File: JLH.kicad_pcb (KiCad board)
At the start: 2 copper layers, 170 x 200 mm, 51 parts, among them J1 Вход, J2 Выход, J3 B2P-VH, Q1 КТ361Г, Q2 КТ801А, Q3 2Т803А, Q4 2Т803А, Q5 КТ361Г, Q6 КТ801А, Q7 2Т803А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

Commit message: Fixed polarity
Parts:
- moved R1 25.1 mm to (87.6, 137.5), turned to 90 degrees
- moved J3 14.8 mm to (76.2, 137.5), turned to 90 degrees
- moved D1 14.5 mm to (73.7, 122.3)
- moved C13 5.00 mm to (102.0, 133.5)
- moved C6 5.00 mm to (102.0, 118.5)
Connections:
- J3 pad 1: /Левый канал/VCC -> GND
- J3 pad 2: GND -> /Левый канал/VCC
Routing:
- net GND: track 666.0 -> 78.9 mm
- net /Левый канал/VCC: track 593.0 -> 575.8 mm
- net Net-(D1-Pad2): track 4.72 -> 11.4 mm
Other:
- board text added: "Левый +"
- board text added: "Левый -"
- board text added: "Правый +"
- board text added: "Правый -"

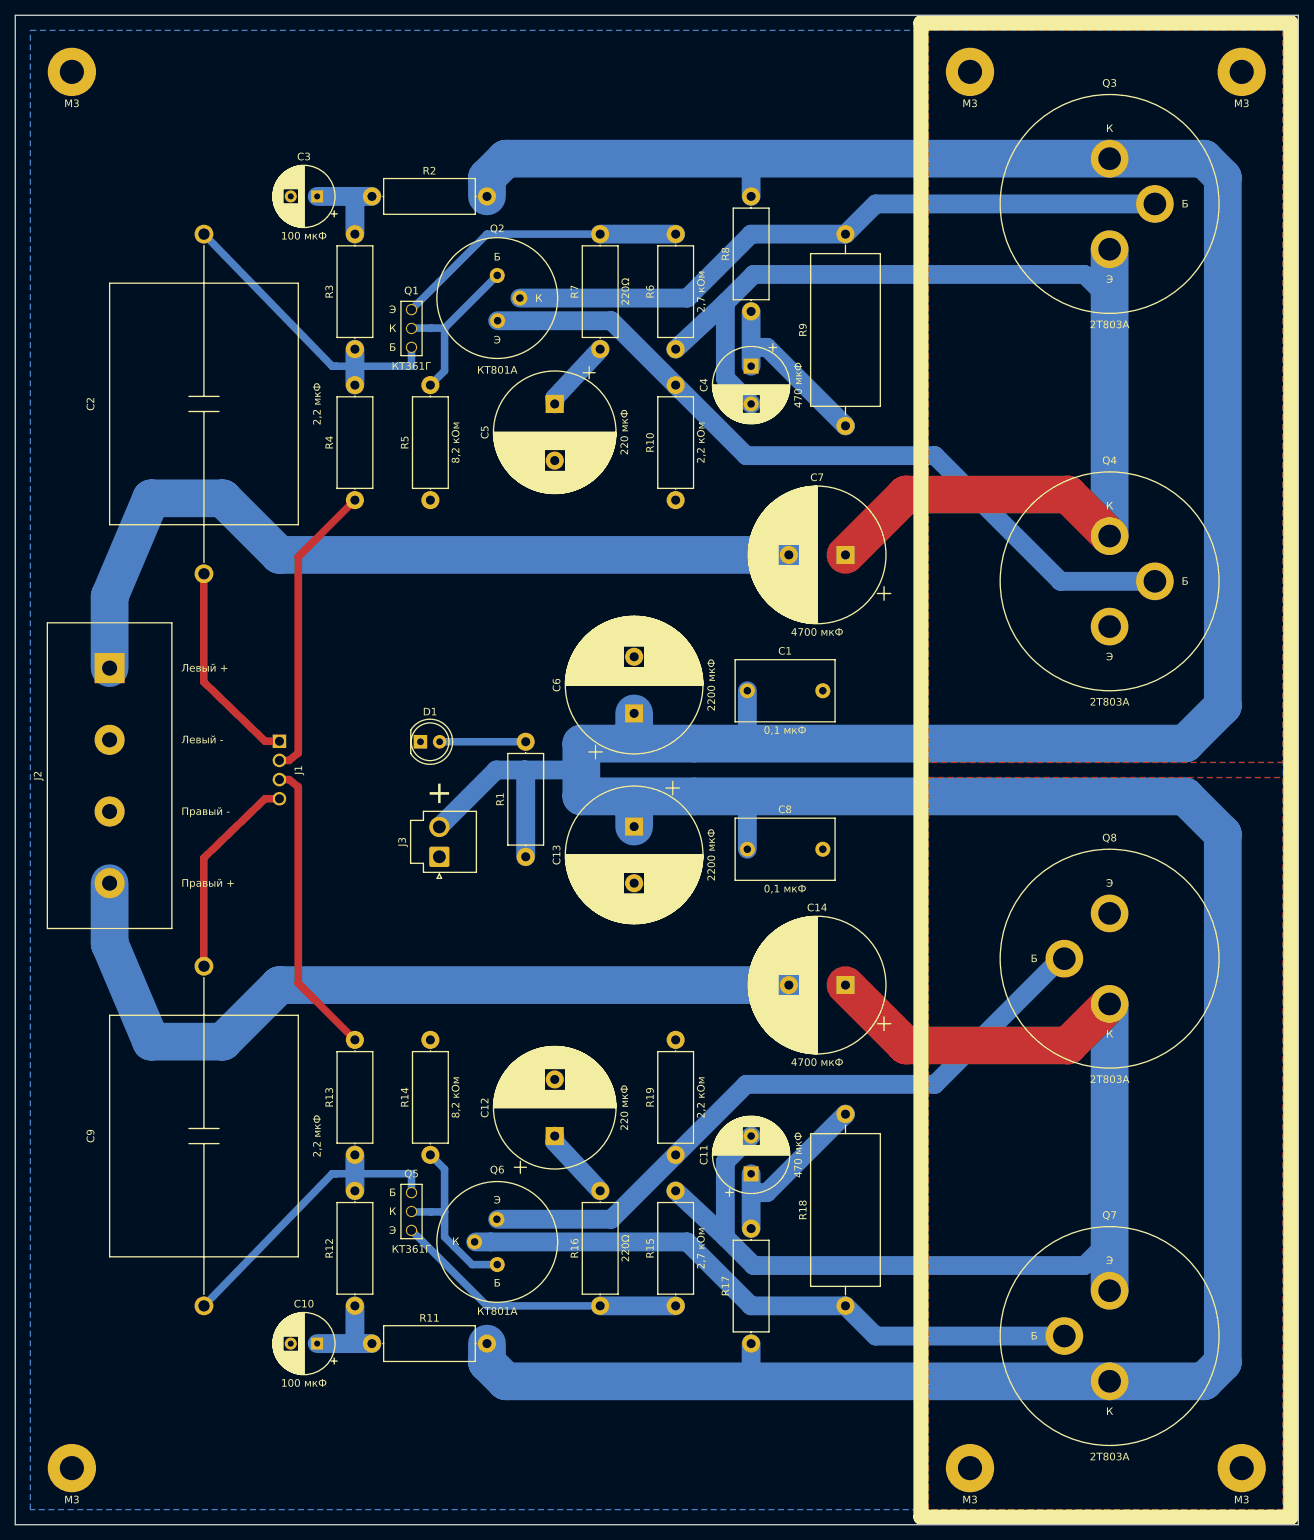
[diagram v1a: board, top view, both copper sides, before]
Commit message: Removed top layer
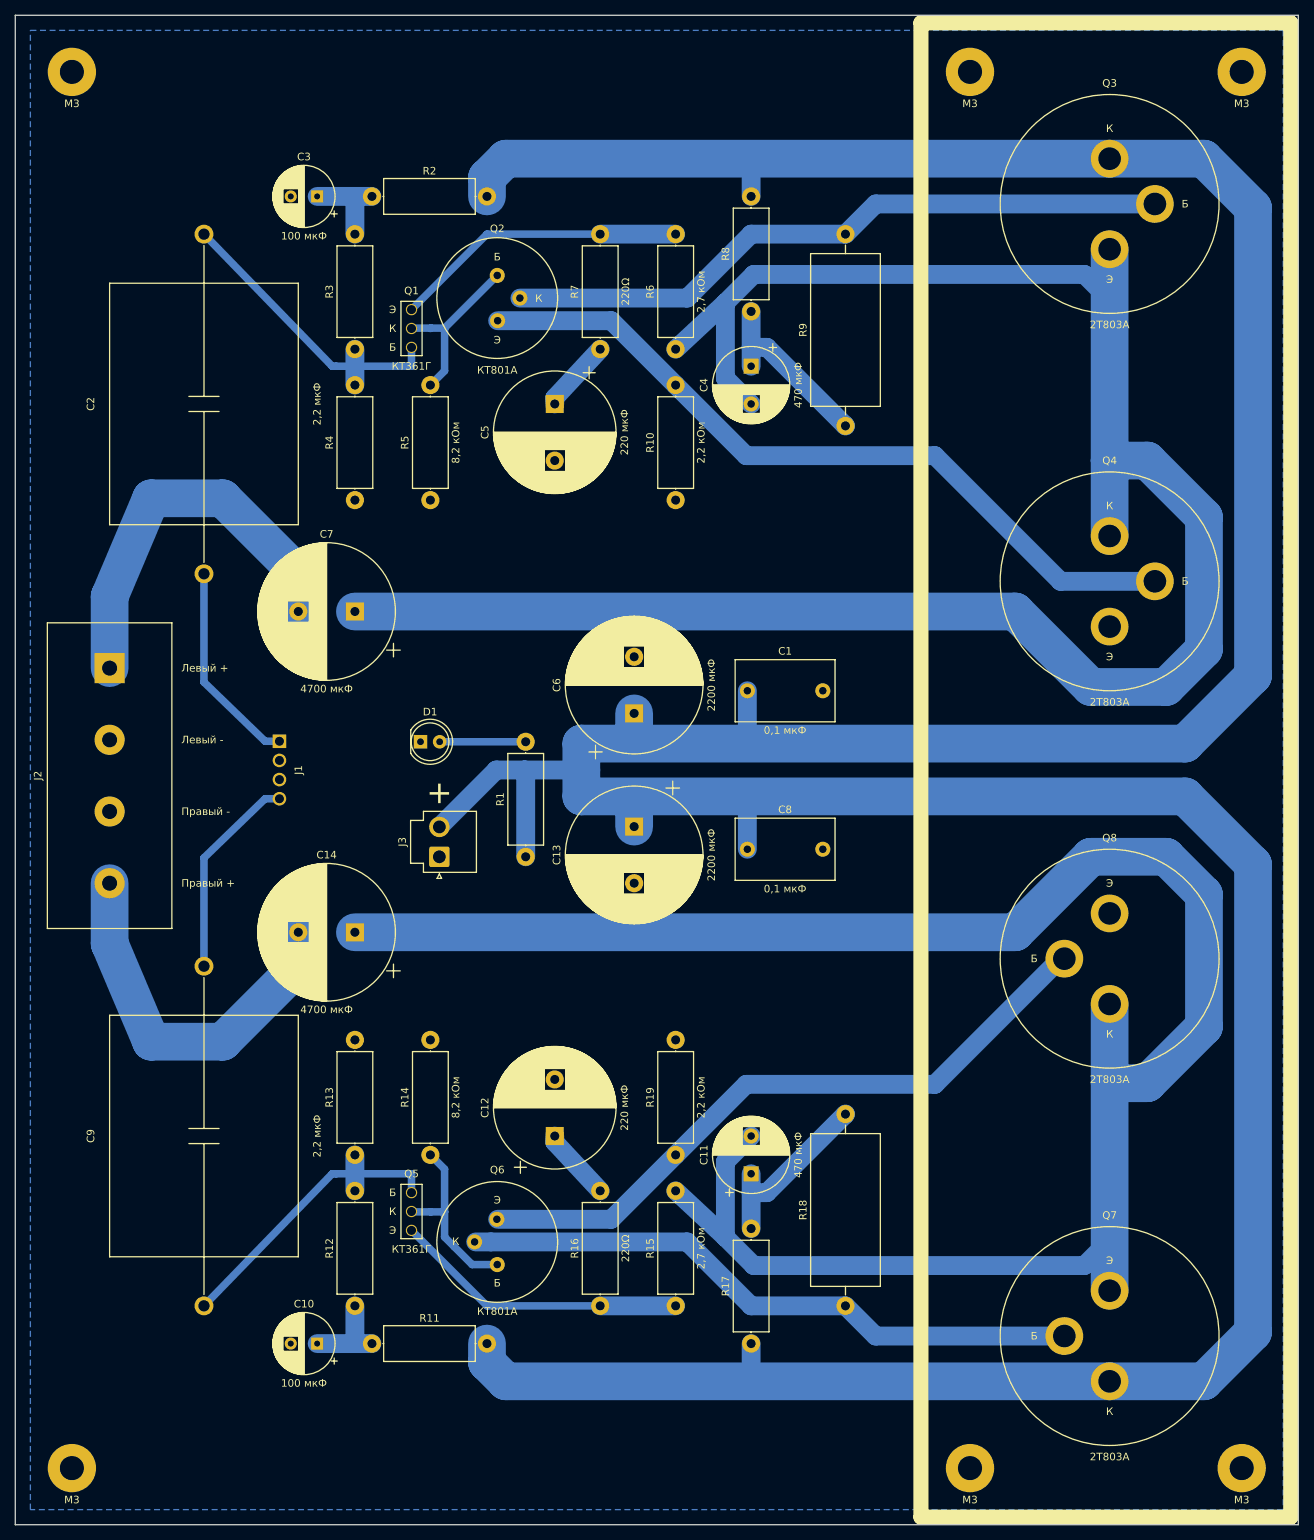
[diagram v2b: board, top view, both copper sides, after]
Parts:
- moved C7 65.4 mm to (65.0, 105.0)
- moved C14 65.4 mm to (65.0, 147.5)
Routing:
- net Net-(C4-Pad2): track 154.6 -> 265.8 mm
- net Net-(C11-Pad2): track 154.6 -> 265.8 mm
- net GND: track 78.9 -> 0.00 mm
- net /Правый канал/OUT+: track 109.7 -> 50.3 mm
- net /Левый канал/OUT+: track 111.2 -> 52.3 mm
- net /Левый канал/VCC: track 575.8 -> 582.4 mm
- removed copper zone on F.Cu, net GND

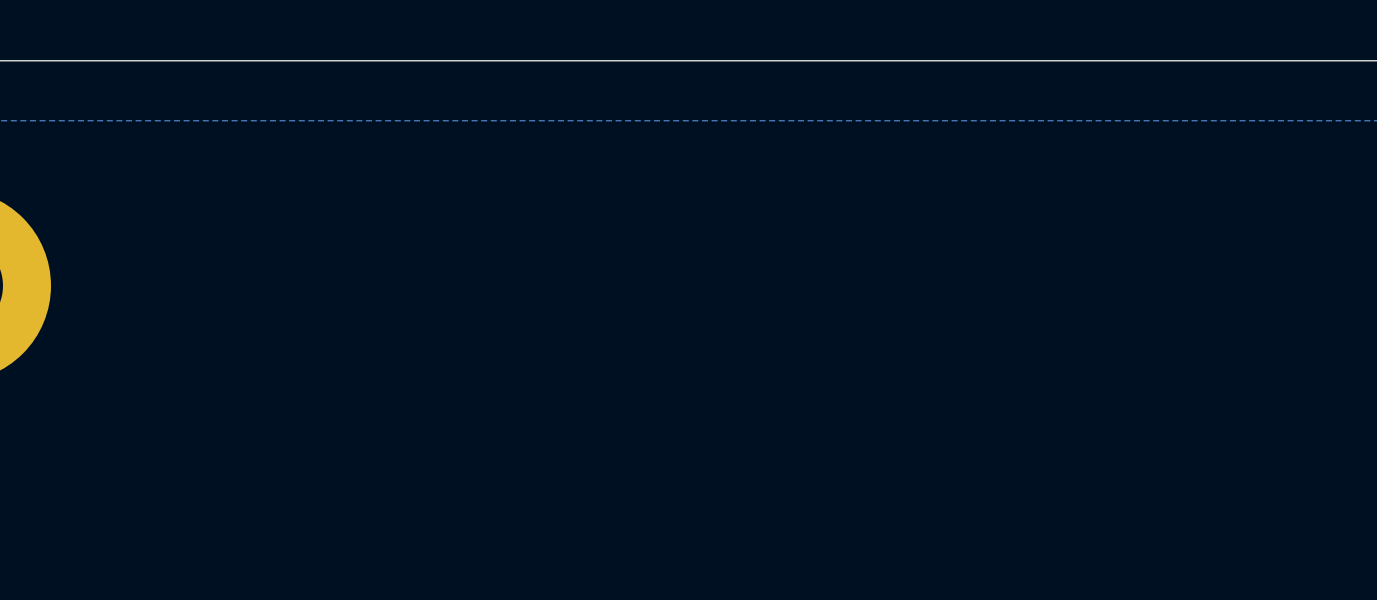
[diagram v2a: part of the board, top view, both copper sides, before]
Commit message: Added author to PCB
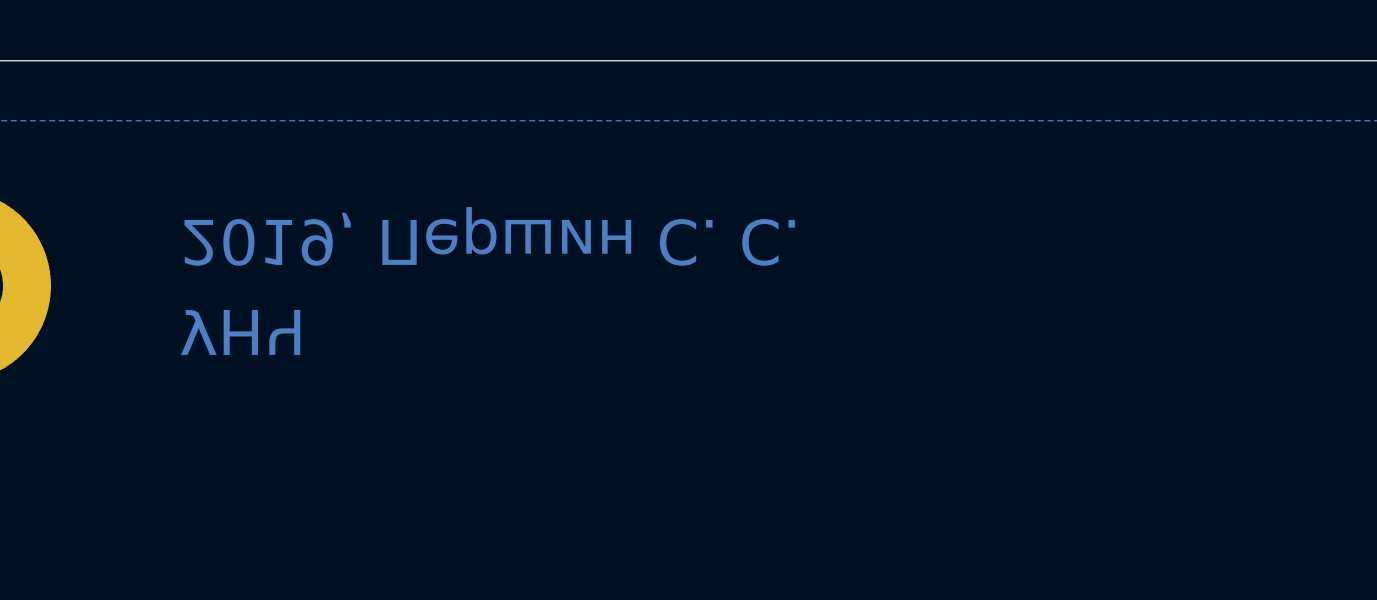
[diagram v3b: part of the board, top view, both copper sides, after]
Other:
- board text added: "2019, Першин С. С."
- board text added: "УНЧ"
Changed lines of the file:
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@@
   (general
     (thickness 1.6)
-    (drawings 22)
+    (drawings 24)
     (tracks 153)
     (zones 0)
@@
     (title "Усилитель JLH")
     (date 2019-07-16)
+    (company "Першин С. С.")
   )
   (layers
@@
     )
   )
+  (gr_text "2019, Першин С. С." (at 35 32 -180) (layer B.Cu)
+    (effects (font (size 1.5 1.5) (thickness 0.3)) (justify left mirror))
+  )
+  (gr_text УНЧ (at 35 35 -180) (layer B.Cu)
+    (effects (font (size 1.5 1.5) (thickness 0.3)) (justify left mirror))
+  )
   (gr_text "Правый +" (at 42 141) (layer F.SilkS)
     (effects (font (size 1 1) (thickness 0.15)) (justify left))
@@
       )
     )
+  )
+  (zone (net 0) (net_name "") (layer B.Cu) (hatch none 0.508)
+    (connect_pads (clearance 0.508))
+    (min_thickness 0.254)
+    (keepout (tracks not_allowed) (vias not_allowed) (copperpour not_allowed))
+    (fill (arc_segments 32) (thermal_gap 0.508) (thermal_bridge_width 0.508))
+    (polygon
+      (pts
+        (xy 33 30) (xy 33 37) (xy 60 37) (xy 60 30)
+      )
+    )
